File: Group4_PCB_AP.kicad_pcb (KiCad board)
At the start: 2 copper layers, 199.9 x 72 mm, 130 parts, among them J1 Conn_02x03_Odd_Even, J10 Conn_Coaxial, J11 Conn_Coaxial, J12 Conn_Coaxial, J13 Conn_02x02_Odd_Even, J14 Conn_02x02_Odd_Even, J15 Conn_02x02_Odd_Even, J16 Conn_02x02_Odd_Even, J17 Conn_02x02_Odd_Even, J18 Conn_Coaxial, J19 Conn_Coaxial, J2 Conn_02x03_Odd_Even, J20 Conn_02x02_Odd_Even, J21 Conn_02x02_Odd_Even, J22 Conn_Coaxial, J23 Conn_Coaxial, J24 Conn_02x02_Odd_Even, J25 Conn_02x02_Odd_Even, J26 Conn_02x02_Odd_Even, J27 Conn_02x02_Odd_Even, J28 Conn_02x02_Odd_Even, J29 Conn_Coaxial, J3 Conn_Coaxial, J30 Conn_Coaxial, J4 Conn_Coaxial, J5 Conn_02x03_Odd_Even, J6 Conn_02x03_Odd_Even, J7 Conn_02x02_Odd_Even, J8 Conn_02x02_Odd_Even, J9 Conn_02x03_Odd_Even

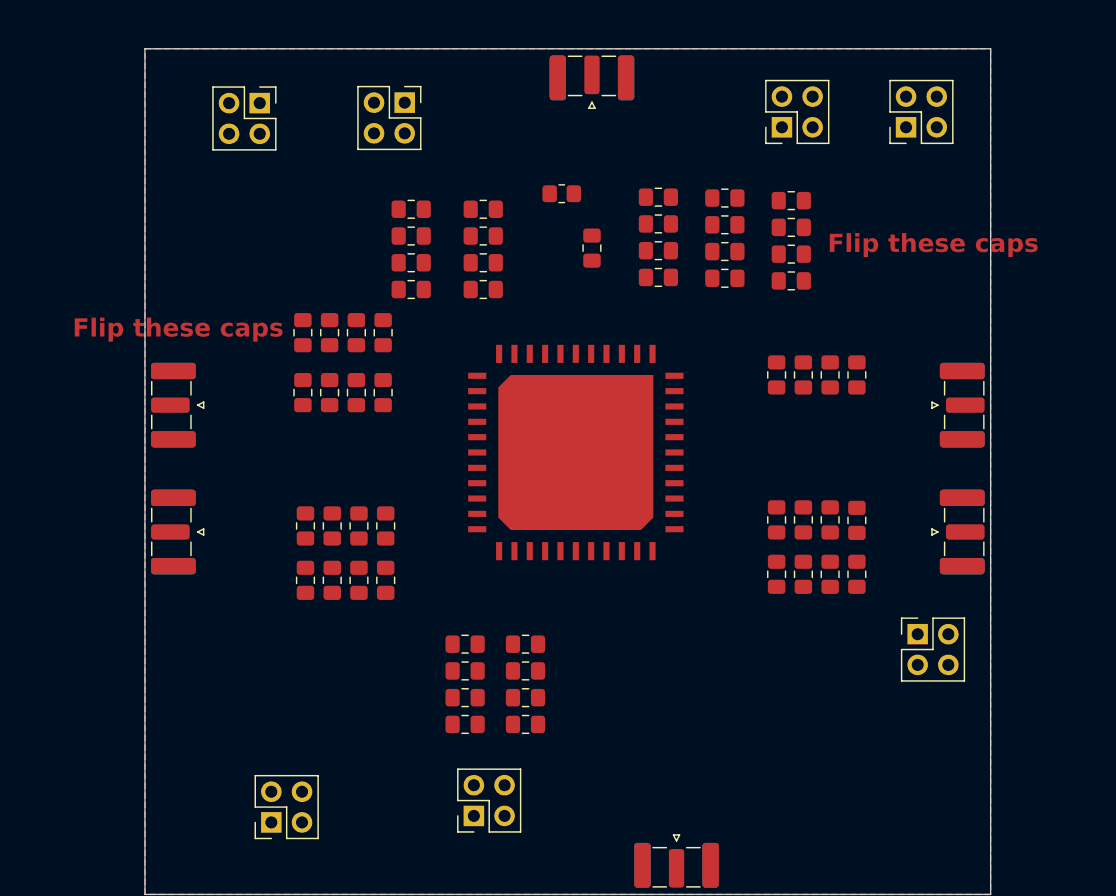
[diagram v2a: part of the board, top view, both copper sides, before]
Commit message: Started routing
Routed almost all nets. Need to finish routing VDD_DIV, GND pour, and matching network
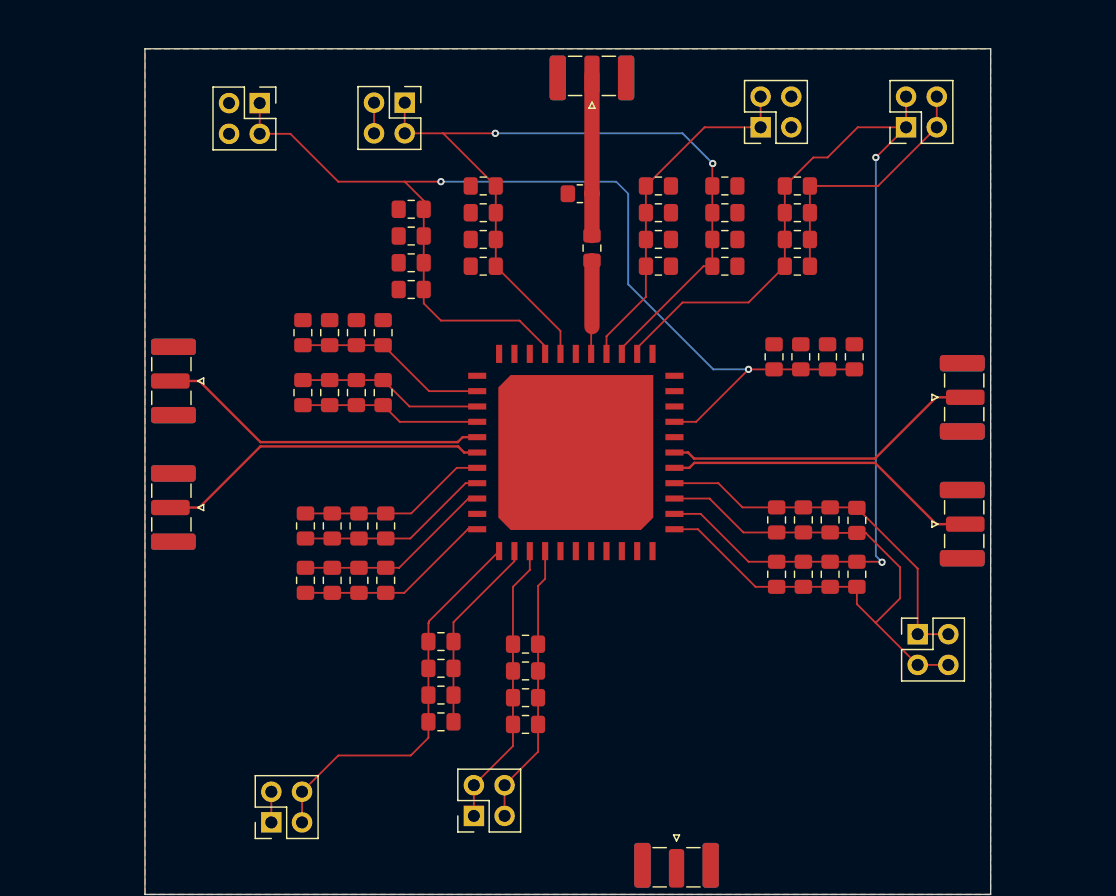
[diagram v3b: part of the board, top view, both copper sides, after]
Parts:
- moved C50 7.87 mm to (224.5, 73.9)
- moved C58 7.64 mm to (218.5, 73.9)
- moved C27 7.57 mm to (213.0, 73.9)
- moved C45 6.64 mm to (190.2, 86.0)
- moved C51 6.64 mm to (183.6, 86.0)
- moved C65 6.64 mm to (190.2, 91.0)
- moved C71 6.64 mm to (183.6, 91.0)
- moved C24 5.71 mm to (213.0, 80.5)
- moved C52 5.64 mm to (218.5, 80.5)
- moved C44 5.45 mm to (224.5, 80.5)
- moved C48 3.46 mm to (224.5, 76.1)
- moved C56 3.21 mm to (218.5, 76.1)
- moved C26 3.14 mm to (213.0, 76.1)
- moved C47 2.21 mm to (188.0, 86.0)
- moved C49 2.21 mm to (185.8, 86.0)
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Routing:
- net /GND: track 83.5 -> 266.2 mm
- net /VDD_DIV: track 0.00 -> 140.3 mm, vias 0 -> 2
- net /VDD_MIX: track 0.00 -> 95.0 mm, vias 0 -> 2
- net /VDD_BB: track 0.00 -> 70.7 mm, vias 0 -> 2
- net /VDD_LNA: track 0.00 -> 34.9 mm
- net /BIAS_LNA: track 0.00 -> 31.0 mm
- net /BIAS_MIXER: track 0.00 -> 29.3 mm
- net /V_BB_Q_N: track 0.00 -> 27.7 mm
- net /V_BB_Q_P: track 0.00 -> 27.7 mm
- net /V_BB_I_N: track 0.00 -> 26.4 mm
- net /V_BB_I_P: track 0.00 -> 26.3 mm
- net /DQ_EN: track 0.00 -> 23.8 mm
- net /CK_CHIP: track 0.00 -> 13.3 mm
- net /CK: track 0.00 -> 7.75 mm
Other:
- board text removed: "Flip these caps"

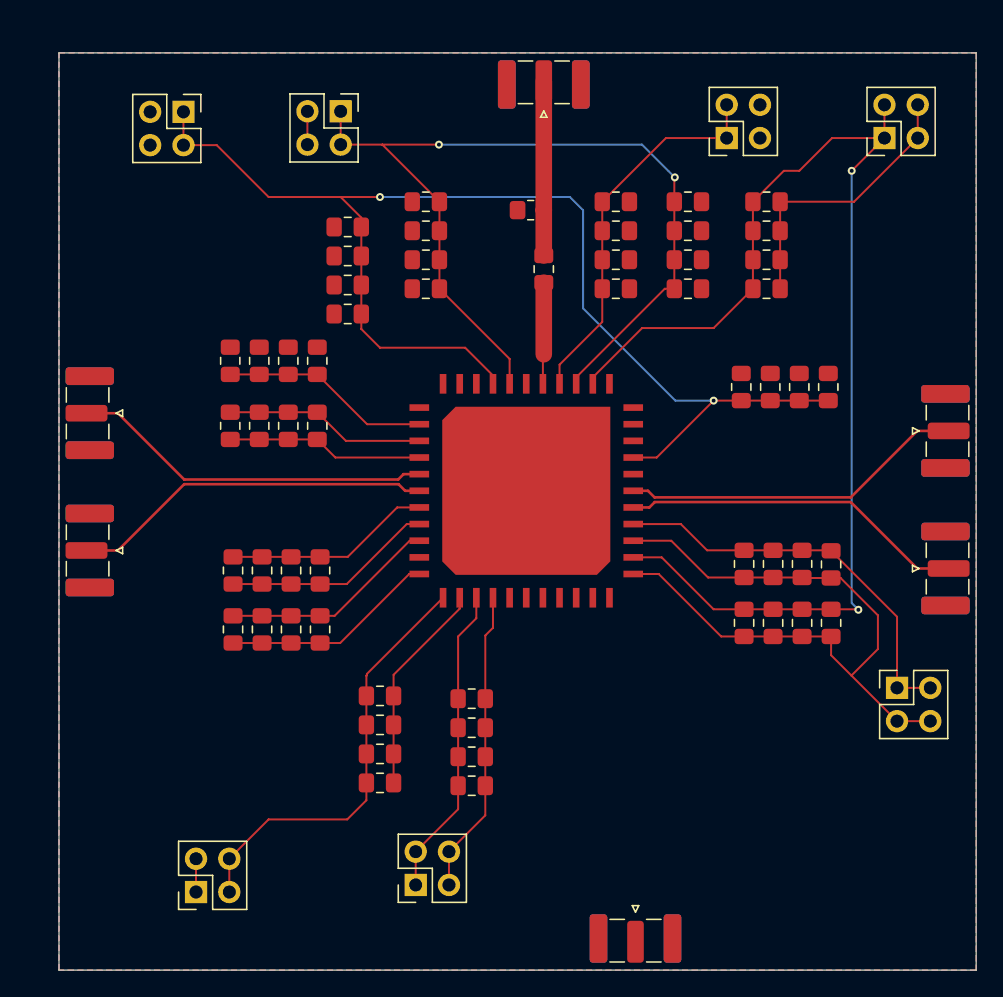
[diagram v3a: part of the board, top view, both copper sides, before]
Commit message: Finished Routing
At 1:35 in video. Finished routing everything. Need to add probe points, via stitching, ID marker, matching network
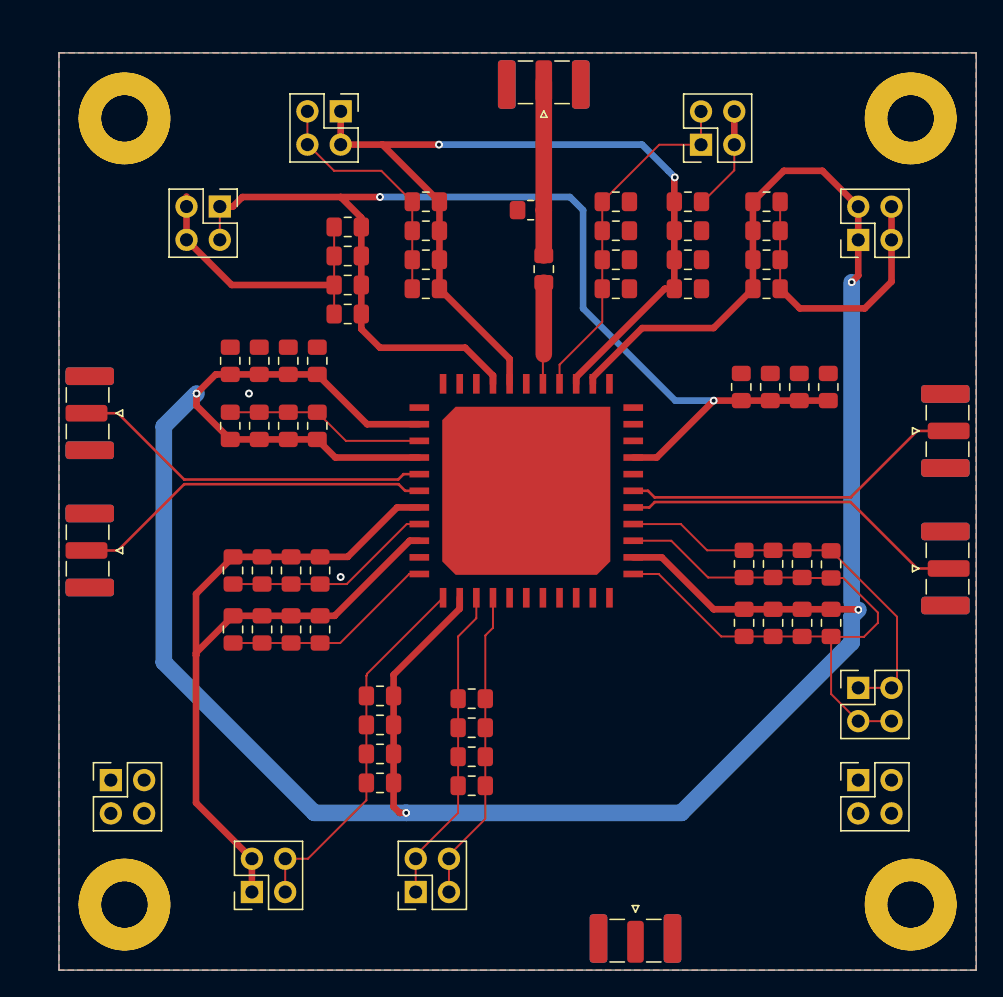
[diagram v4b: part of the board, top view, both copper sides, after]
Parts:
- added ? (x2): , , F.Cu at (175.5, 67.5)
- added ? (x2): , , F.Cu at (235.5, 127.5)
- added ?: , , F.Cu at (238.0, 65.0)
- added ?: , , F.Cu at (235.5, 67.5)
- added ? (x2): , , F.Cu at (175.5, 127.5)
- added J31: Conn_02x02_Odd_Even, Connector_PinHeader_2.54mm:PinHeader_2x02_P2.54mm_Vertical, F.Cu at (231.5, 118.0)
- added J32: Conn_02x02_Odd_Even, Connector_PinHeader_2.54mm:PinHeader_2x02_P2.54mm_Vertical, F.Cu at (174.5, 118.0)
- moved J26 8.03 mm to (231.5, 76.8)
- moved J25 7.74 mm to (182.8, 74.2)
- moved J24 4.26 mm to (185.2, 126.5)
- moved J20 2.96 mm to (231.5, 111.0)
- moved J21 2.03 mm to (219.5, 69.5)
- moved J28 0.54 mm to (197.7, 126.5)
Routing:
- net /VDD_DIV: track 140.3 -> 227.4 mm, vias 2 -> 4
- net /GND: track 266.2 -> 308.0 mm, vias 879 -> 881
- net /VDD_LNA: track 34.9 -> 65.1 mm
- net /VDD_MIX: track 95.0 -> 90.9 mm
- net /BIAS_MIXER: track 29.3 -> 27.1 mm

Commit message: Additions to schematic and layout
Added coupling cap for RF input
Added matching network with zero ohm resistors to detach it
Added zero ohm resistors to VDD lines.
Need to add probe points, via stitches, and ID
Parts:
- added C76: 1n, Capacitor_SMD:C_0805_2012Metric_Pad1.18x1.45mm_HandSolder, F.Cu at (212.0, 121.5)
- added C80: 1n, Capacitor_SMD:C_0805_2012Metric_Pad1.18x1.45mm_HandSolder, F.Cu at (217.0, 108.0)
- added C81: 1n, Capacitor_SMD:C_0805_2012Metric_Pad1.18x1.45mm_HandSolder, F.Cu at (221.0, 118.0)
- added J33: Conn_02x02_Odd_Even, Connector_PinHeader_2.54mm:PinHeader_2x02_P2.54mm_Vertical, F.Cu at (176.0, 77.5)
- added L1: 3n, Capacitor_SMD:C_0603_1608Metric_Pad1.08x0.95mm_HandSolder, F.Cu at (208.5, 112.5)
- added L2: 3n, Capacitor_SMD:C_0603_1608Metric_Pad1.08x0.95mm_HandSolder, F.Cu at (212.0, 112.5)
- added L3: 3n, Capacitor_SMD:C_0603_1608Metric_Pad1.08x0.95mm_HandSolder, F.Cu at (215.5, 112.5)
- added R20: 51, Resistor_SMD:R_0805_2012Metric_Pad1.20x1.40mm_HandSolder, F.Cu at (214.0, 125.0)
- added R21: 0, Resistor_SMD:R_0805_2012Metric_Pad1.20x1.40mm_HandSolder, F.Cu at (212.0, 108.0)
- added R22: 0, Resistor_SMD:R_0805_2012Metric_Pad1.20x1.40mm_HandSolder, F.Cu at (216.0, 118.0)
- added R23: 0, Resistor_SMD:R_0805_2012Metric_Pad1.20x1.40mm_HandSolder, F.Cu at (219.5, 112.5)
- added R24: 0, Resistor_SMD:R_0603_1608Metric_Pad0.98x0.95mm_HandSolder, F.Cu at (175.5, 110.0)
- added R25: 0, Resistor_SMD:R_0603_1608Metric_Pad0.98x0.95mm_HandSolder, F.Cu at (184.0, 67.5)
- added R26: 0, Resistor_SMD:R_0603_1608Metric_Pad0.98x0.95mm_HandSolder, F.Cu at (184.5, 71.0)
- added R27: 0, Resistor_SMD:R_0603_1608Metric_Pad0.98x0.95mm_HandSolder, F.Cu at (178.0, 85.5)
- moved J19 2.50 mm to (212.0, 130.3)
- moved J27 2.33 mm to (191.8, 69.3), turned to 180 degrees
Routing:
- net /VDD: track 219.4 -> 269.9 mm, vias 0 -> 2
- net /VIN_RF_S: track 0.00 -> 24.0 mm
- net /VIN_RF: track 0.00 -> 21.1 mm
- net /GND: track 308.0 -> 298.6 mm
- net /SMA_VIN_RF: track 0.00 -> 7.80 mm
- net /VDD_LNA: track 65.1 -> 71.8 mm
- net /VDD_BB: track 70.7 -> 76.1 mm
- net /VDD_MIX: track 90.9 -> 94.5 mm
- net /VC2: track 0.00 -> 2.96 mm
- net /VC1: track 0.00 -> 2.96 mm
- net /VDD_DIV: track 227.4 -> 225.1 mm

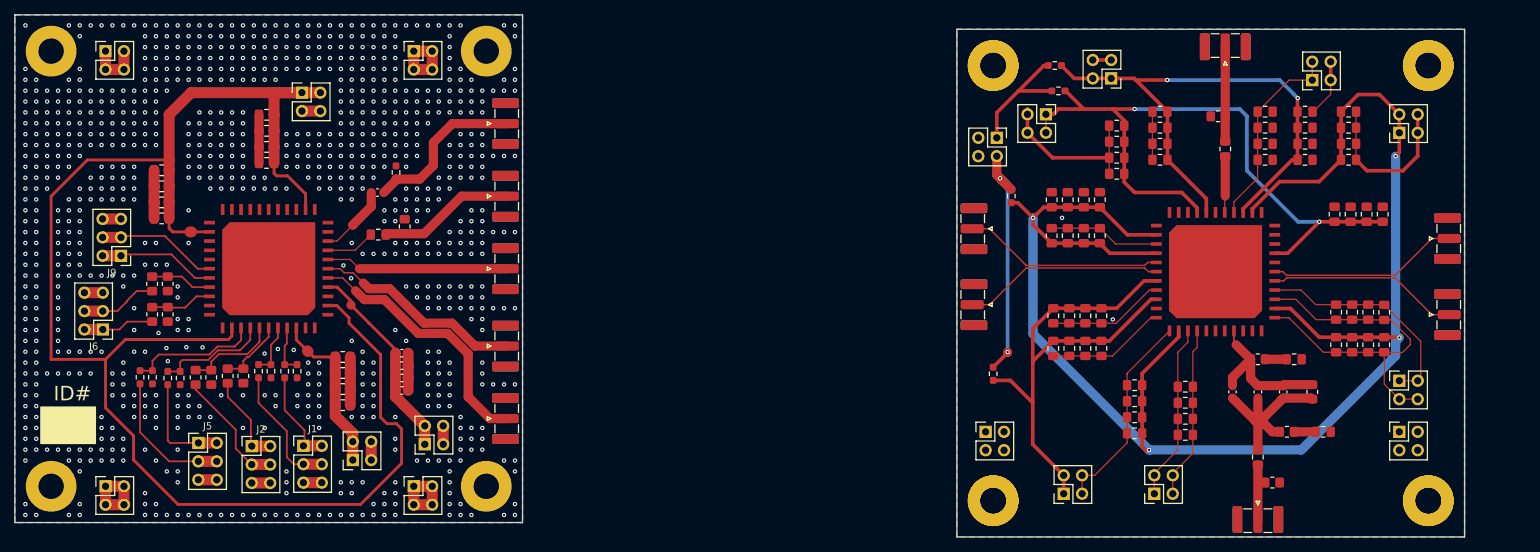
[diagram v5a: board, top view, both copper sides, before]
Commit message: updated matching nw, added probe points, via stitching. TODO: fix DRC errors
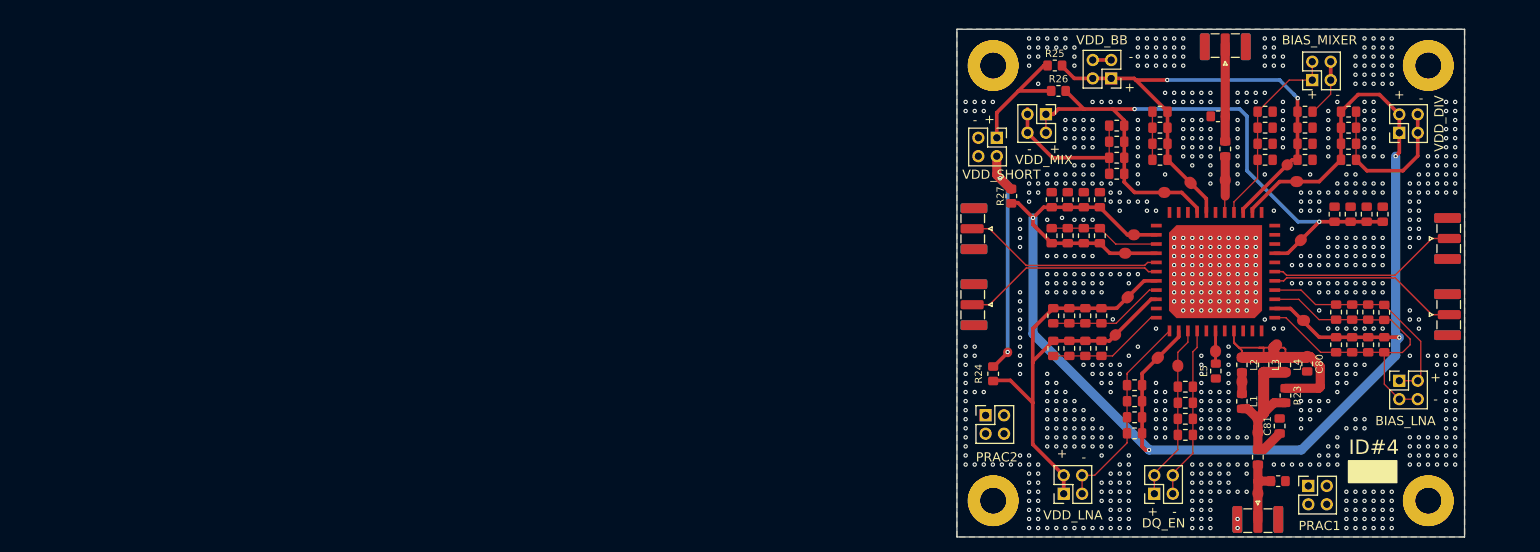
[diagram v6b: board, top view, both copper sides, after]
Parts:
- removed the ? at (45.6, 65.5)
- removed the ? at (45.6, 125.5)
- removed the ? at (108.1, 63.0)
- removed the ? at (105.6, 125.5)
- removed C1, C4: 1n, Capacitor_SMD:C_0603_1608Metric_Pad1.08x0.95mm_HandSolder
- removed C10, C14, C18: 22u, Capacitor_SMD:C_0805_2012Metric_Pad1.18x1.45mm_HandSolder
- removed C11, C15, C7: 22p, Capacitor_SMD:C_0805_2012Metric_Pad1.18x1.45mm_HandSolder
- removed C12, C16, C8: 2.2n, Capacitor_SMD:C_0805_2012Metric_Pad1.18x1.45mm_HandSolder
- removed C13, C17, C9: 0.22u, Capacitor_SMD:C_0805_2012Metric_Pad1.18x1.45mm_HandSolder
- removed C2: 1n, Capacitor_SMD:C_0805_2012Metric_Pad1.18x1.45mm_HandSolder
- removed C3: 10p, Capacitor_SMD:C_0603_1608Metric_Pad1.08x0.95mm_HandSolder
- removed C5: 0.1u, Capacitor_SMD:C_0603_1608Metric_Pad1.08x0.95mm_HandSolder
- removed C6: 10u, Capacitor_SMD:C_0603_1608Metric_Pad1.08x0.95mm_HandSolder
- removed J1, J2, J5, J6, J9: Conn_02x03_Odd_Even, Connector_PinHeader_2.54mm:PinHeader_2x03_P2.54mm_Vertical
- removed J10, J11, J12, J3, J4: Conn_Coaxial, Connector_Coaxial:SMA_Samtec_SMA-J-P-H-ST-EM1_EdgeMount
- removed J13, J14, J15, J16, J17, J7, J8: Conn_02x02_Odd_Even, Connector_PinHeader_2.54mm:PinHeader_2x02_P2.54mm_Vertical
- removed R1, R2, R3, R4: 1K, Resistor_SMD:R_0603_1608Metric_Pad0.98x0.95mm_HandSolder
- removed R10: 51, Resistor_SMD:R_0805_2012Metric_Pad1.20x1.40mm_HandSolder
- removed R11, R13: 1.2K, Resistor_SMD:R_0603_1608Metric_Pad0.98x0.95mm_HandSolder
- removed R12, R14: 2.2K, Resistor_SMD:R_0603_1608Metric_Pad0.98x0.95mm_HandSolder
- removed R15, R17: 1.2K, Resistor_SMD:R_0805_2012Metric_Pad1.20x1.40mm_HandSolder
- removed R16, R18: 2.2K, Resistor_SMD:R_0805_2012Metric_Pad1.20x1.40mm_HandSolder
- removed R21, R22: 0, Resistor_SMD:R_0805_2012Metric_Pad1.20x1.40mm_HandSolder
- removed R5, R6, R7, R8: 1K, Resistor_SMD:R_0805_2012Metric_Pad1.20x1.40mm_HandSolder
- removed R9: 51, Resistor_SMD:R_0603_1608Metric_Pad0.98x0.95mm_HandSolder
- removed the U1 at (75.6, 95.5)
- added L4: L, Inductor_SMD:L_0805_2012Metric_Pad1.15x1.40mm_HandSolder, F.Cu at (215.8, 108.8)
- added L5: L, Inductor_SMD:L_0805_2012Metric_Pad1.15x1.40mm_HandSolder, F.Cu at (206.2, 109.6)
- L1, L2, L3: value 3n -> L; footprint Capacitor_SMD:C_0603_1608Metric_Pad1.08x0.95mm_HandSolder -> Inductor_SMD:L_0805_2012Metric_Pad1.15x1.40mm_HandSolder
- R19, R20: value 51 -> 50
- R24, R25, R26, R27: footprint Resistor_SMD:R_0603_1608Metric_Pad0.98x0.95mm_HandSolder -> Resistor_SMD:R_0805_2012Metric_Pad1.20x1.40mm_HandSolder
- moved J31 14.6 mm to (219.0, 125.5)
- moved C81 6.05 mm to (215.0, 117.2), turned to 90 degrees
- moved L3 4.60 mm to (212.8, 108.8), turned to -90 degrees
- moved L2 4.33 mm to (209.8, 108.8), turned to -90 degrees
- moved R23 3.73 mm to (215.8, 113.0)
- moved J32 2.28 mm to (174.5, 115.7)
- moved C80 1.91 mm to (218.8, 108.6), turned to -90 degrees
- moved L1 1.84 mm to (209.8, 113.8), turned to -90 degrees
- moved R20 0.82 mm to (214.8, 124.8)
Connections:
- C80 pad 1: /VC2 -> /VIN_RF
- C81 pad 1: /VC1 -> /VIN_RF_S
- L1 pad 1: /VIN_RF_S -> Net-(L1-Pad1)
- L1 pad 2: /VIN_RF -> /VIN_RF_S
- L2 pad 1: /VIN_RF_S -> /VIN_RF
- L2 pad 2: /VIN_RF -> Net-(L1-Pad1)
- L3 pad 1: /VIN_RF_S -> /VIN_RF
- L3 pad 2: /VIN_RF -> /VIN_RF_S
- U1 pad 12: /GND -> /VSOURCE
- U1 pad 13: /GND -> /VSOURCE
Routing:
- net /VDD: track 269.9 -> 50.5 mm
- net /GND: track 298.6 -> 215.1 mm, vias 881 -> 845
- net /SMA_DIFF_N: track 36.2 -> 0.00 mm
- net /SMA_DIFF_P: track 29.2 -> 0.00 mm
- net /VDD_0603: track 28.0 -> 0.00 mm
- net /SMA_SE: track 25.3 -> 0.00 mm
- net /VDD_0805: track 23.2 -> 0.00 mm
- net /SMA_SB_0603_IN: track 22.9 -> 0.00 mm
- net /SMA_SB_0805_IN: track 19.0 -> 0.00 mm
- net /C1_5V: track 18.9 -> 0.00 mm
- net /C1_1p8V: track 18.2 -> 0.00 mm
- net /A1_3p3V: track 17.8 -> 0.00 mm
- net /B1_3p3V: track 16.8 -> 0.00 mm
- net /E1: track 16.7 -> 0.00 mm
- net /E0: track 16.2 -> 0.00 mm
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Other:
- board size 199.9 x 72 mm -> 70 x 70 mm
- board text added: "ID#4"
- board text removed: "ID#"
